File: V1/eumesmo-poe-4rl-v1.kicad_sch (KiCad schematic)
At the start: 56 parts, among them J1 USB_C_Receptacle_USB2.0, J2 RJ45 JACK, Q1 UMH3N, Q2 WPM2015-3/TR, Q3 LMUN2211LT1G, SW1 RESET, U1 CH340K, U2 ESP32-WROOM-32UE-N16, U3 LAN8710A

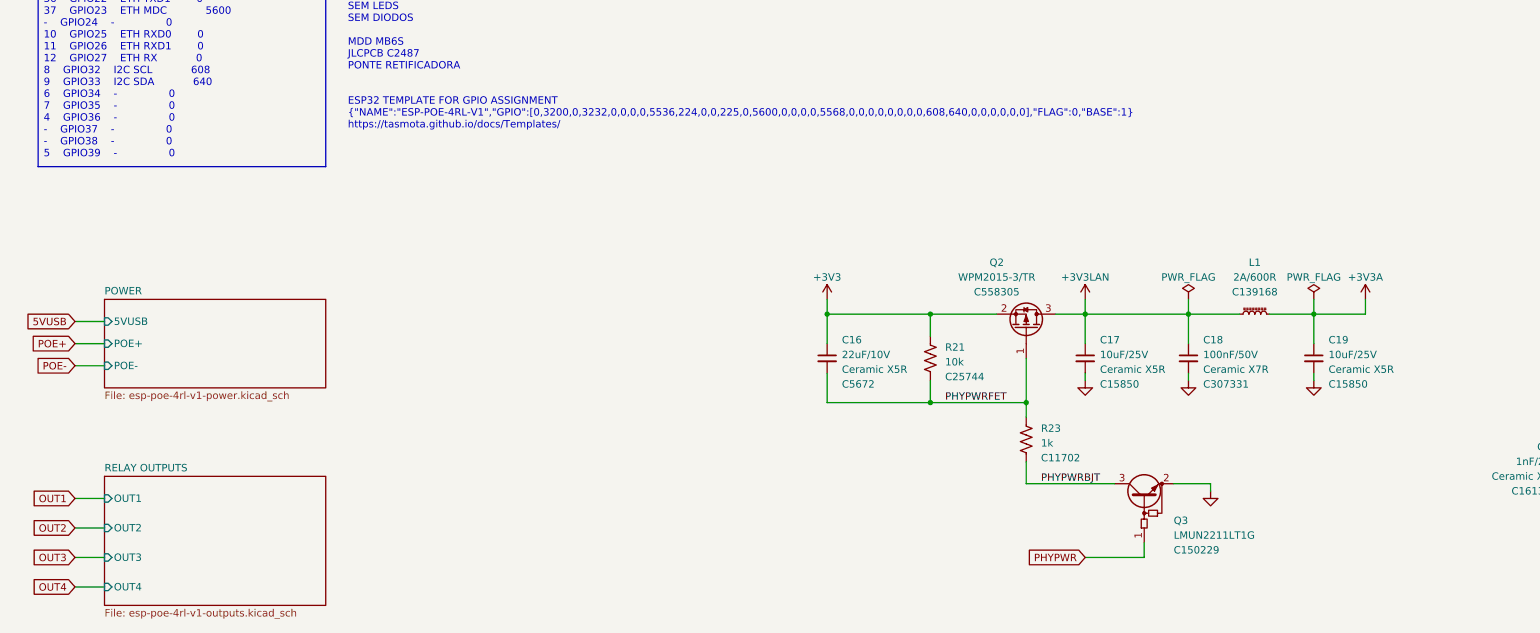
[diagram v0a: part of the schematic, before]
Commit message: Renamed all files to align with eumesmo branding.
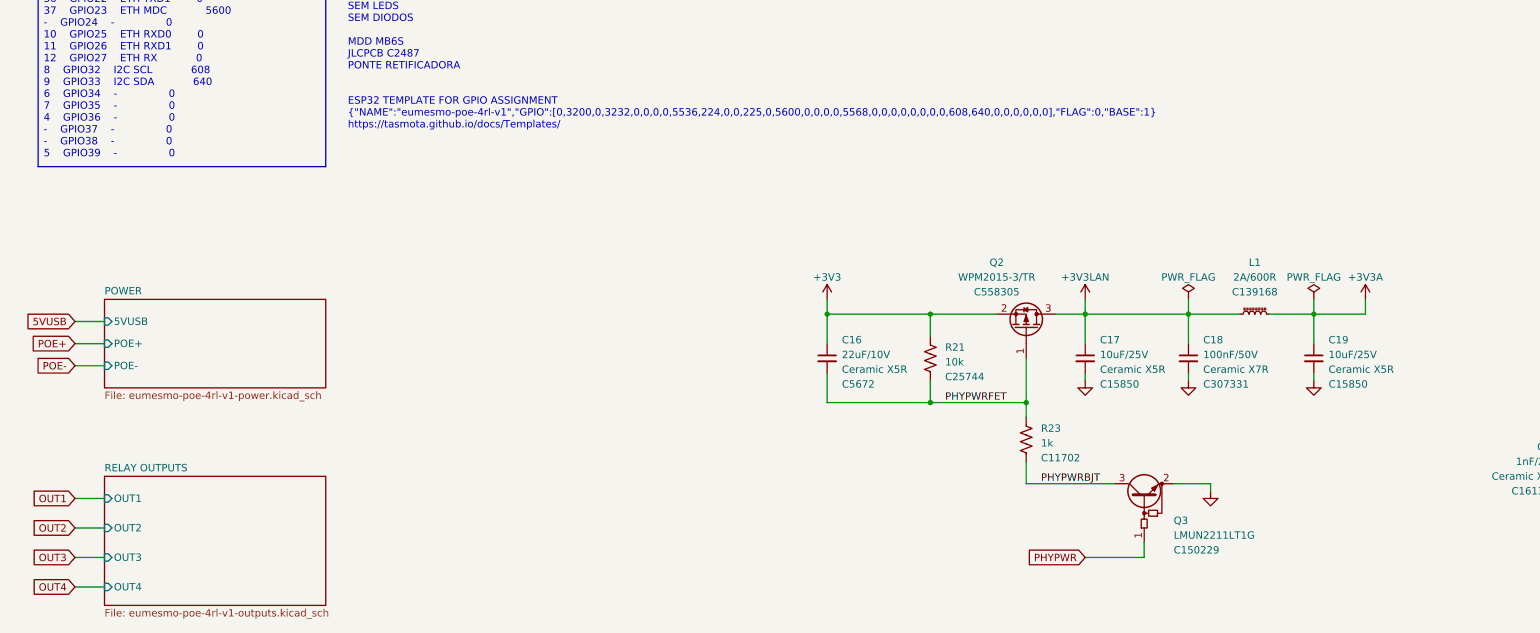
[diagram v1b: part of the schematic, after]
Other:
- sheet POWER: file esp-poe-4rl-v1-power.kicad_sch -> eumesmo-poe-4rl-v1-power.kicad_sch
- sheet RELAY OUTPUTS: file esp-poe-4rl-v1-outputs.kicad_sch -> eumesmo-poe-4rl-v1-outputs.kicad_sch
- note added: "ESP32 TEMPLATE FOR GPIO ASSIGNMENT {"NAME":"eumesmo-poe-4rl-v1","GPIO":[0,3200,0,3232,0,0,0,0,5536,224,0,0,225,0,5600,0,0,0,0,5568,0,0,0,0,0,0,0,0,608,640,0,0,0,0,0,0],"FLAG":0,"BASE":1} https://tasmota.github.io/docs/Templates/"
- note removed: "ESP32 TEMPLATE FOR GPIO ASSIGNMENT {"NAME":"ESP-POE-4RL-V1","GPIO":[0,3200,0,3232,0,0,0,0,5536,224,0,0,225,0,5600,0,0,0,0,5568,0,0,0,0,0,0,0,0,608,640,0,0,0,0,0,0],"FLAG":0,"BASE":1} https://tasmota.github.io/docs/Templates/"
- title: ESP 4x Relay Output Module with PoE -> eumesmo 4x Relay Output Module with PoE

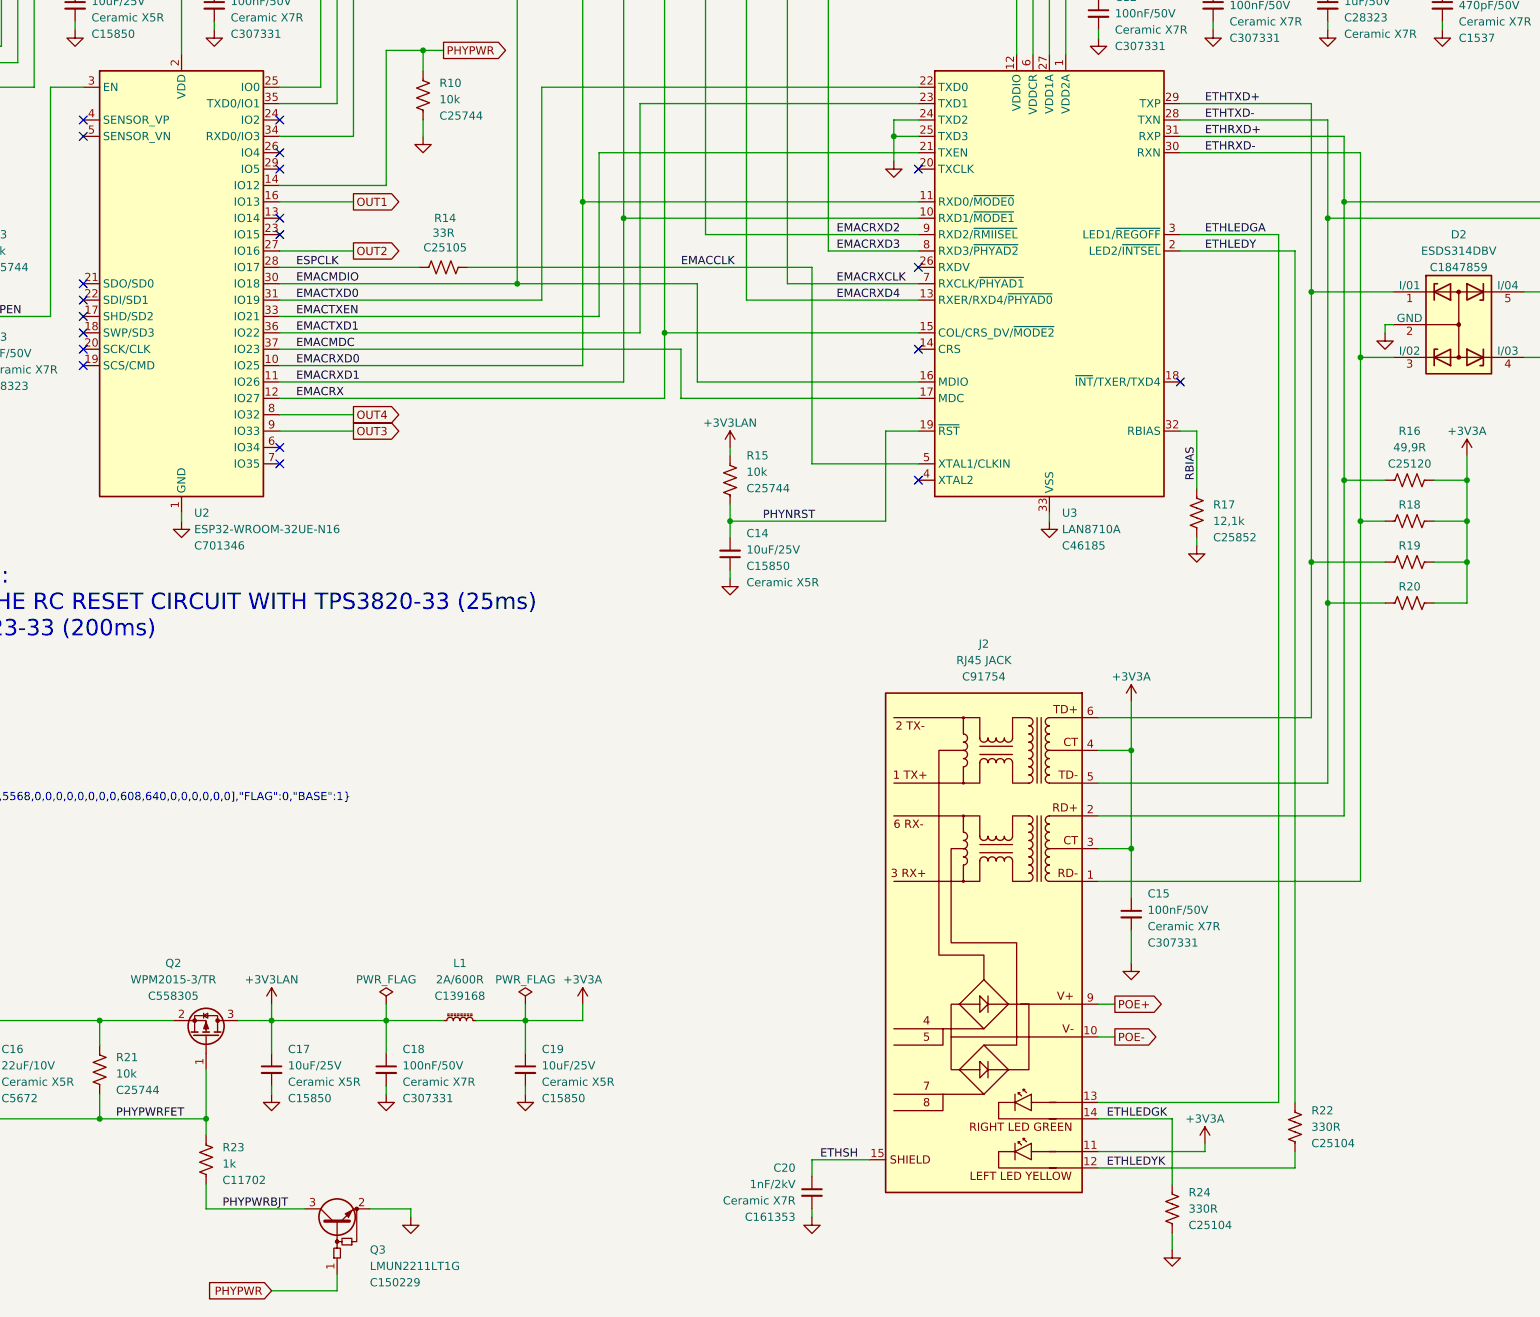
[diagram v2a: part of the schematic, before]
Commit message: Added CPU health LED
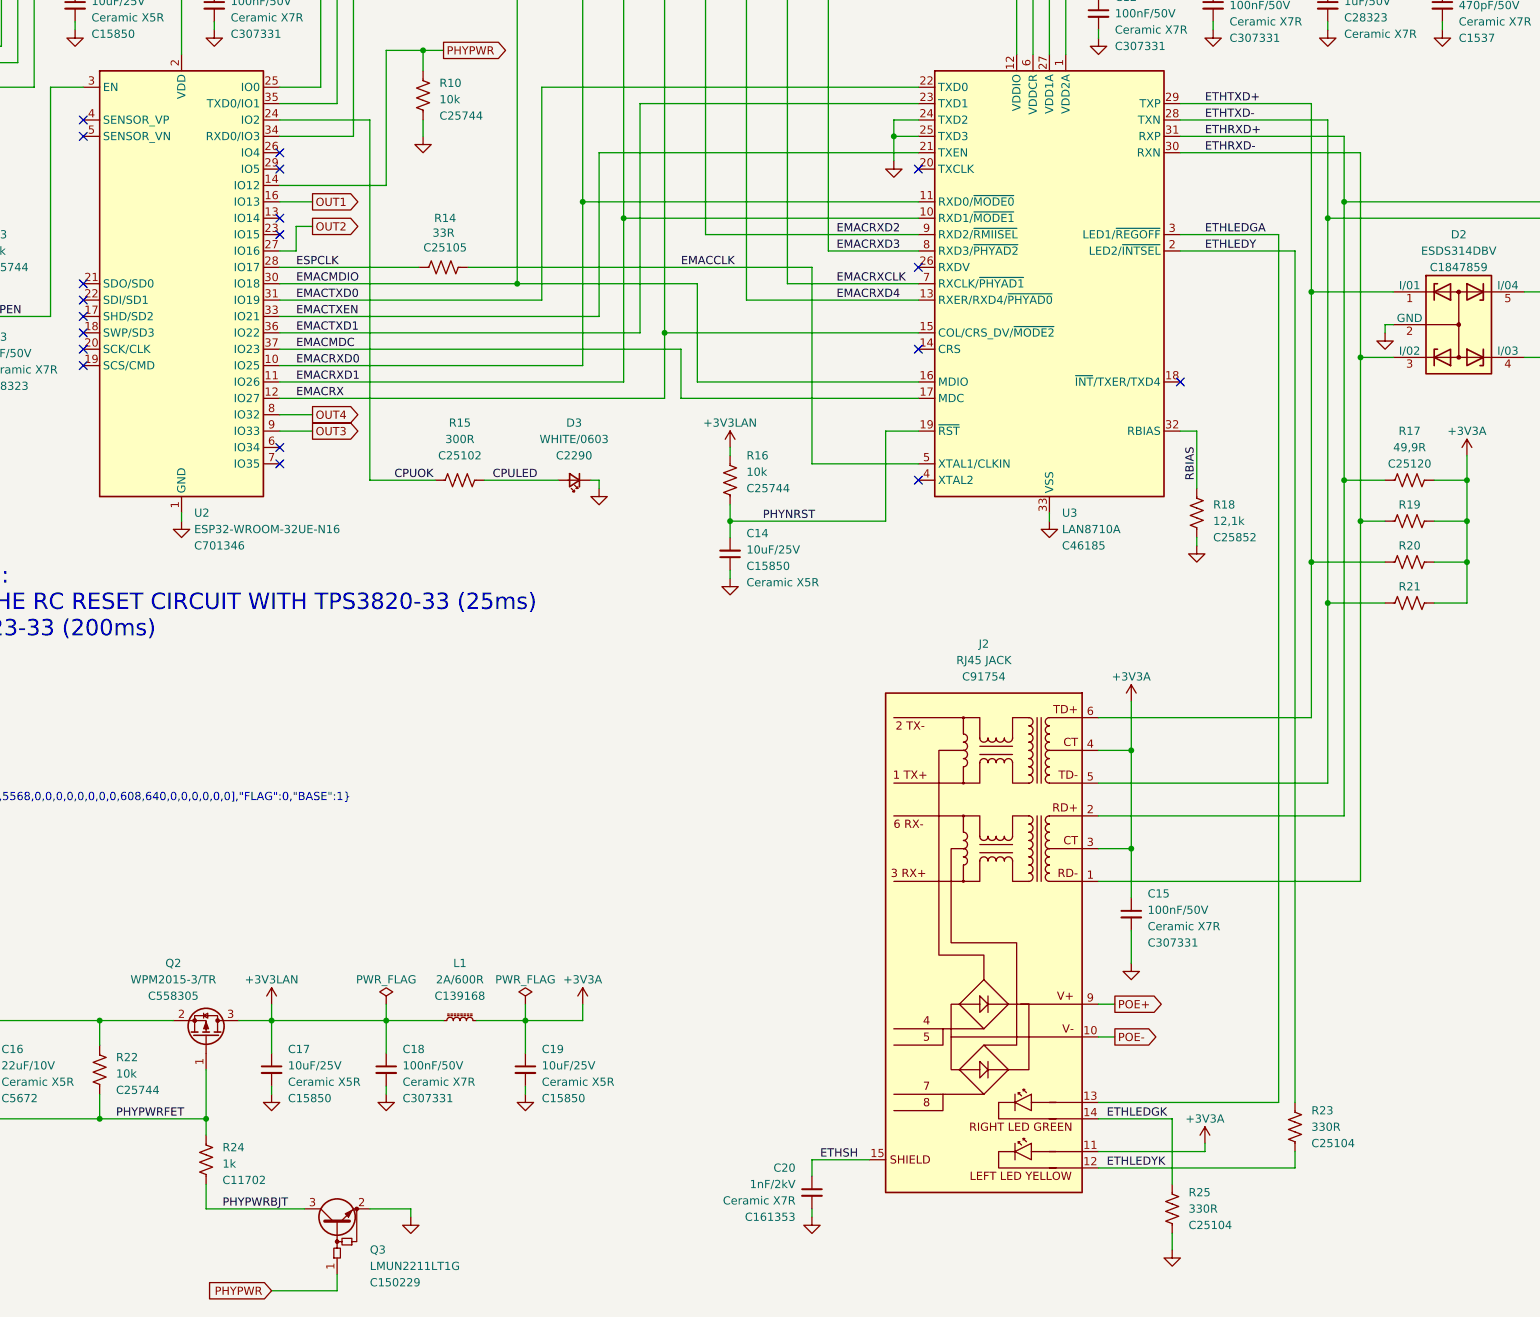
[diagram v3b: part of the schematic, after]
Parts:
- added D3: WHITE/0603, Tales:LED_0603_1608Metric, symbol Device:LED_Small
- added R15: 300R, Tales:R_0402_1005Metric, symbol Device:R_US
- renumbered R15 to R16, R16 to R17, R17 to R18, R18 to R19, R19 to R20, R20 to R21, R21 to R22, R22 to R23, R23 to R24, R24 to R25
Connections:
- net GND: now also D3.1 (K)
- net CPUOK: now reaches U2.24 (IO2)
- net CPUOK: now also R15.1
- new net CPULED: D3.2 (A), R15.2
- no-connect marks 23 -> 22
